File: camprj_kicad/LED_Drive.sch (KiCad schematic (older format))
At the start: 0 parts

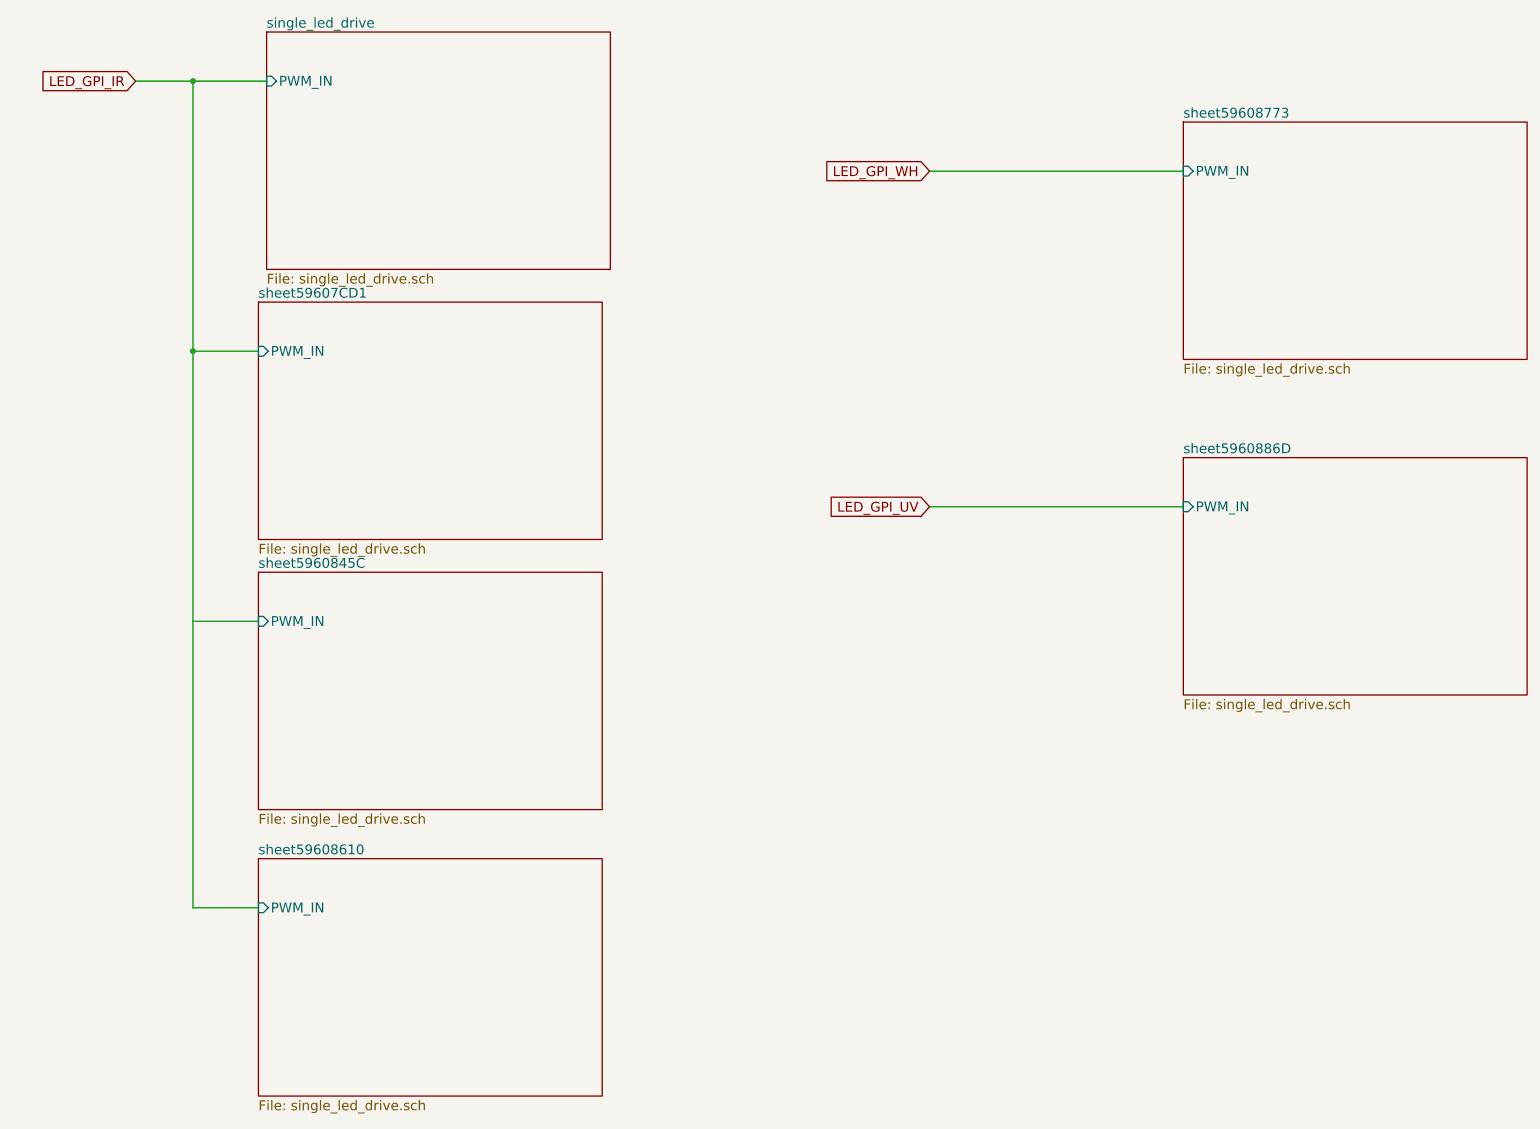
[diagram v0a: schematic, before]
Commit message: Board design: component placement done
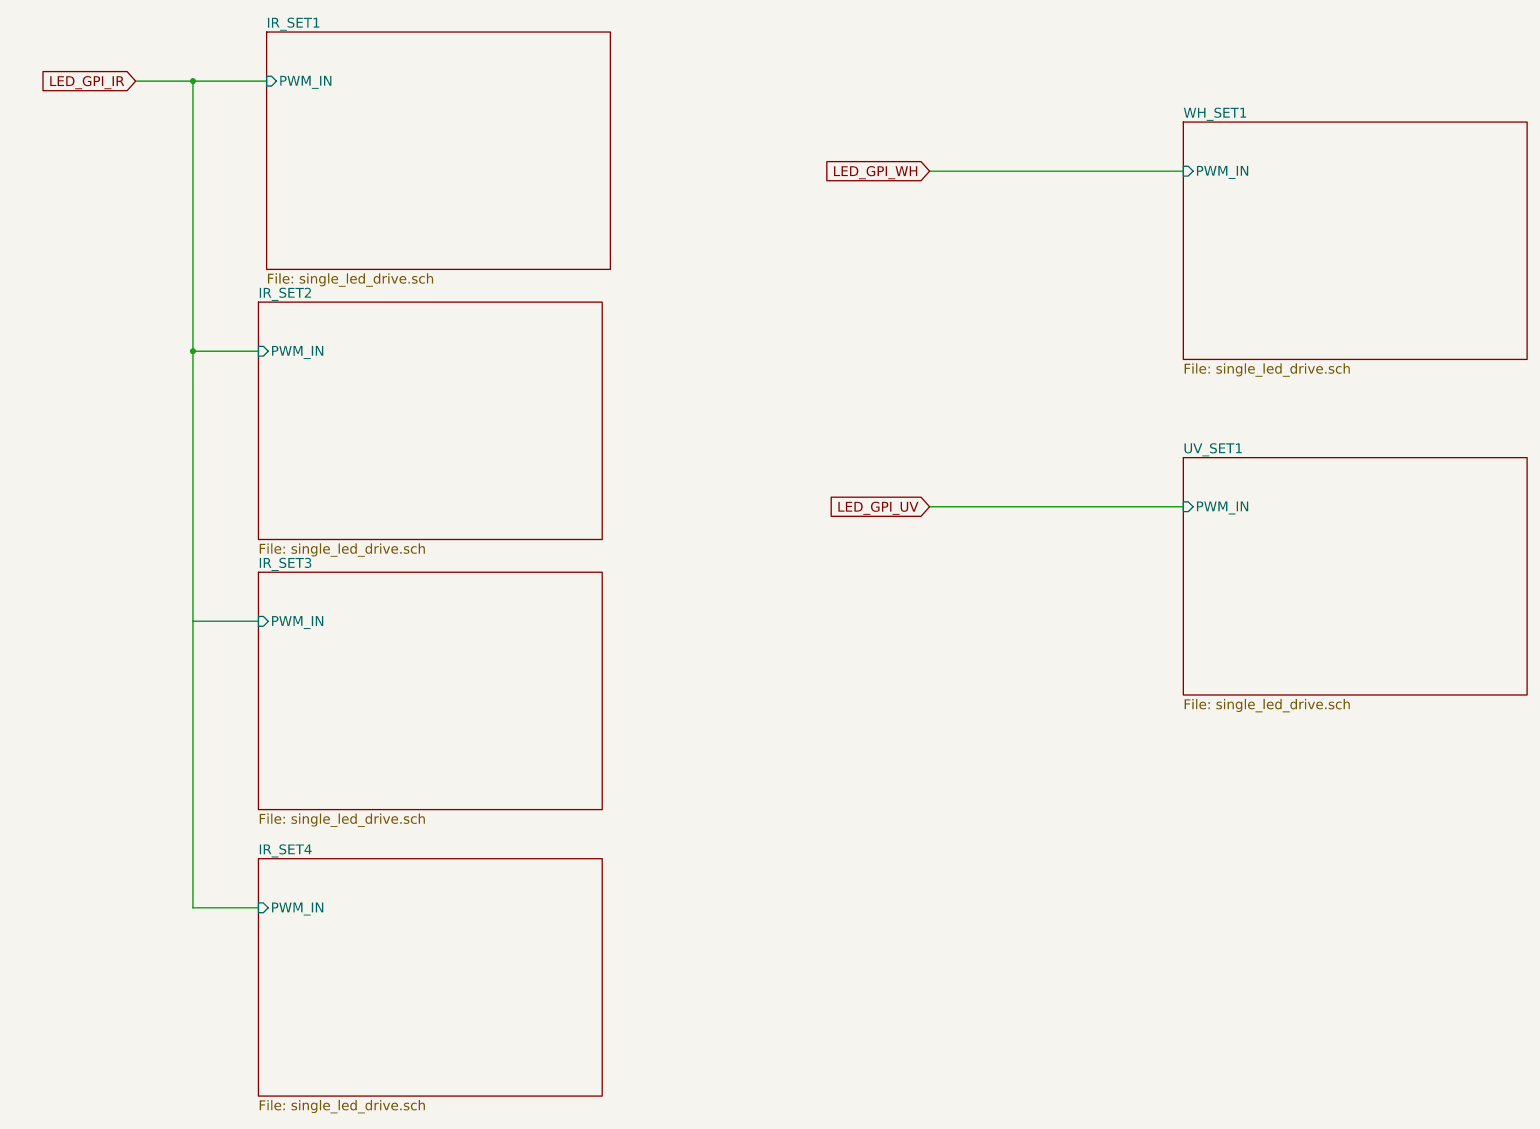
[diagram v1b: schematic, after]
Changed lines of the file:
@@
 EESchema Schematic File Version 2
+LIBS:camprj_kicad-rescue
 LIBS:power
 LIBS:device
@@
 S 2150 700  2100 1450
 U 59604F09
-F0 "single_led_drive" 60
+F0 "IR_SET1" 60
 F1 "single_led_drive.sch" 60
 F2 "PWM_IN" I L 2150 1000 60
@@
 S 2100 2350 2100 1450
 U 59607CD4
-F0 "sheet59607CD1" 60
+F0 "IR_SET2" 60
 F1 "single_led_drive.sch" 60
 F2 "PWM_IN" I L 2100 2650 60
@@
 S 2100 4000 2100 1450
 U 5960845F
-F0 "sheet5960845C" 60
+F0 "IR_SET3" 60
 F1 "single_led_drive.sch" 60
 F2 "PWM_IN" I L 2100 4300 60
@@
 S 2100 5750 2100 1450
 U 59608613
-F0 "sheet59608610" 60
+F0 "IR_SET4" 60
 F1 "single_led_drive.sch" 60
 F2 "PWM_IN" I L 2100 6050 60
@@
 S 7750 1250 2100 1450
 U 59608776
-F0 "sheet59608773" 60
+F0 "WH_SET1" 60
 F1 "single_led_drive.sch" 60
 F2 "PWM_IN" I L 7750 1550 60
@@
 S 7750 3300 2100 1450
 U 59608870
-F0 "sheet5960886D" 60
+F0 "UV_SET1" 60
 F1 "single_led_drive.sch" 60
 F2 "PWM_IN" I L 7750 3600 60
